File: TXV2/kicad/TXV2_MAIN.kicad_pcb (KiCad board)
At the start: 2 copper layers, 83.3 x 91.7 mm, 58 parts, among them J1 USB-C, J10 TRIMS, J11 WS2812, J12 QWIIC, J13 I2C, J14 RTC, J15 ESP-A, J16 ESP-B, J17 BUZZ, J2 NEXTION, J3 BATT, J4 BAL, J5 BTN, J6 GIMBAL L, J7 GIMBAL R, J8 KNOBS, J9 SWITCHES, U1 Teensy 4.1, U2 ESP32-S3-DevKitC, U3 nRF24 PA/LNA, U4 Pololu 2808, U5 5V buck, U7 BQ25887, U8 AMS1117-3.3

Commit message: TXV2 rev-A: assembly-clarity silk — USB-end arrows + pin-1 markers on both MCUs, per-pin function labels (Nextion GND/skip/5V/RX/TX, buck VIN/GND/VOUT, XT30 +/-), spare headers renamed 'ESP32 SPARE GPIO A/B', Pololu flagged CHECK PINOUT
Co-Authored-By: Claude Fable 5 <noreply@anthropic.com>
Claude-Session: https://claude.ai/code/session_01DvvNNevU4xtNTYtdVBAM7h
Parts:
- J15: value ESP-A -> ESP32 SPARE GPIO (A)
- J16: value ESP-B -> ESP32 SPARE GPIO (B)
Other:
- board text added: "(skip)"
- board text added: "+"
- board text added: "-"
- board text added: "1"
- board text added: "2"
- board text added: "3"
- board text added: "3V3"
- board text added: "4"
- board text added: "5"
- board text added: "5V"
- board text added: "6"
- board text added: "7"
- board text added: "8"
- board text added: "<<< USB END (ESP32)"
- board text added: "<<< USB END (TEENSY)"
- board text added: "BTN"
- board text added: "BUZ"
- board text added: "G"
- board text added: "GND"
- board text added: "LED"
- board text added: "MID"
- board text added: "PWR LATCH - CHECK PINOUT"
- board text added: "RX"
- board text added: "SCL"
- board text added: "SDA"
- board text added: "TX"
- board text added: "VB"
- board text added: "VIN"
- board text added: "VOUT"

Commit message: TXV2 rev-A: corrected board routed (keyed 2808 + dual buck split rail), function-name silk re-applied
Co-Authored-By: Claude Fable 5 <noreply@anthropic.com>
Claude-Session: https://claude.ai/code/session_01DvvNNevU4xtNTYtdVBAM7h
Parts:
- added R17: 47k, Resistor_SMD:R_0805_2012Metric, F.Cu at (116.0, 166.0)
- added R18: 15k, Resistor_SMD:R_0805_2012Metric, F.Cu at (116.0, 170.0)
- added U9: 5V buck NEXT, TXV2:Buck3pin_VGV, F.Cu at (111.0, 172.0)
- U5: value 5V buck -> 5V buck MAIN; footprint TXV2:Buck5V_Socket -> TXV2:Buck3pin_VGV
- moved U5 7.62 mm to (111.0, 164.0), turned to 90 degrees
- moved C11 6.40 mm to (122.0, 142.0)
- moved R15 5.00 mm to (116.0, 142.0)
- moved R16 4.47 mm to (119.0, 142.0)
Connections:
- J1 pad SH: GND -> (no net)
- J2 pad 3: +5V -> +5V_NEXT
- U4 pad 2: GND -> VBAT_RAW
- U4 pad 3: VBAT_SW -> GND
- U4 pad 4: PWRBTN -> GND
- U4 pad 5: (no net) -> PWR_ON
- U4 pad 6: (no net) -> LATCH_OFF
- U4 pad 7: LATCH_OFF -> CTRL_TP
- U4 pad 8: (no net) -> VBAT_SW
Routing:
- net TRIM7: track 116.0 -> 0.00 mm, vias 5 -> 0
- net I2C_SCL: track 240.0 -> 138.0 mm
- net +5V_NEXT: track 0.00 -> 96.3 mm, vias 0 -> 2
- net CHG_STAT: track 73.1 -> 0.00 mm, vias 5 -> 0
- net TRIM8: track 114.0 -> 45.2 mm, vias 6 -> 0
- net LINK_TX2: track 82.2 -> 23.0 mm, vias 3 -> 0
- net VBAT_SW: track 38.6 -> 86.1 mm
- net CHG_TS: track 96.9 -> 50.0 mm, vias 6 -> 4
- net GND: track 38.8 -> 0.00 mm, vias 189 -> 0
- net +3V3_T: track 236.0 -> 203.7 mm
- net PWR_ON: track 0.00 -> 25.3 mm, vias 0 -> 1
- net TRIM6: track 95.7 -> 70.7 mm, vias 5 -> 6
- net PWRBTN: track 92.1 -> 114.6 mm
- net CB_PATH: track 24.0 -> 3.50 mm, vias 2 -> 0
- net I2C_SDA: track 114.7 -> 134.8 mm, vias 7 -> 4
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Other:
- board text added: "PWR LATCH (2808)"
- board text removed: "PWR LATCH - CHECK PINOUT"

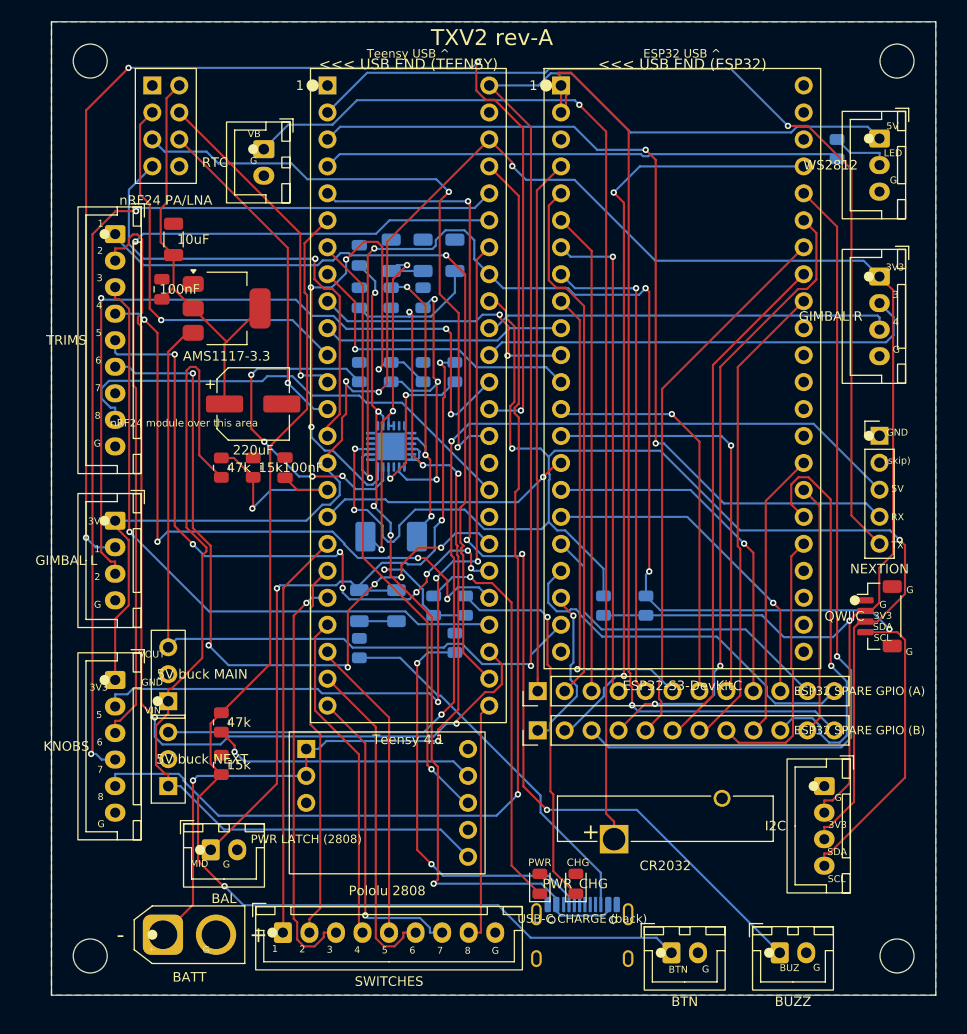
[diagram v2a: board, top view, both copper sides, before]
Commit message: TXV2 rev-A: complete design incl. soft-power diodes, routed ~95% (last ~11 short links + GND stitch for interactive finish before gerbers)
Co-Authored-By: Claude Fable 5 <noreply@anthropic.com>
Claude-Session: https://claude.ai/code/session_01DvvNNevU4xtNTYtdVBAM7h
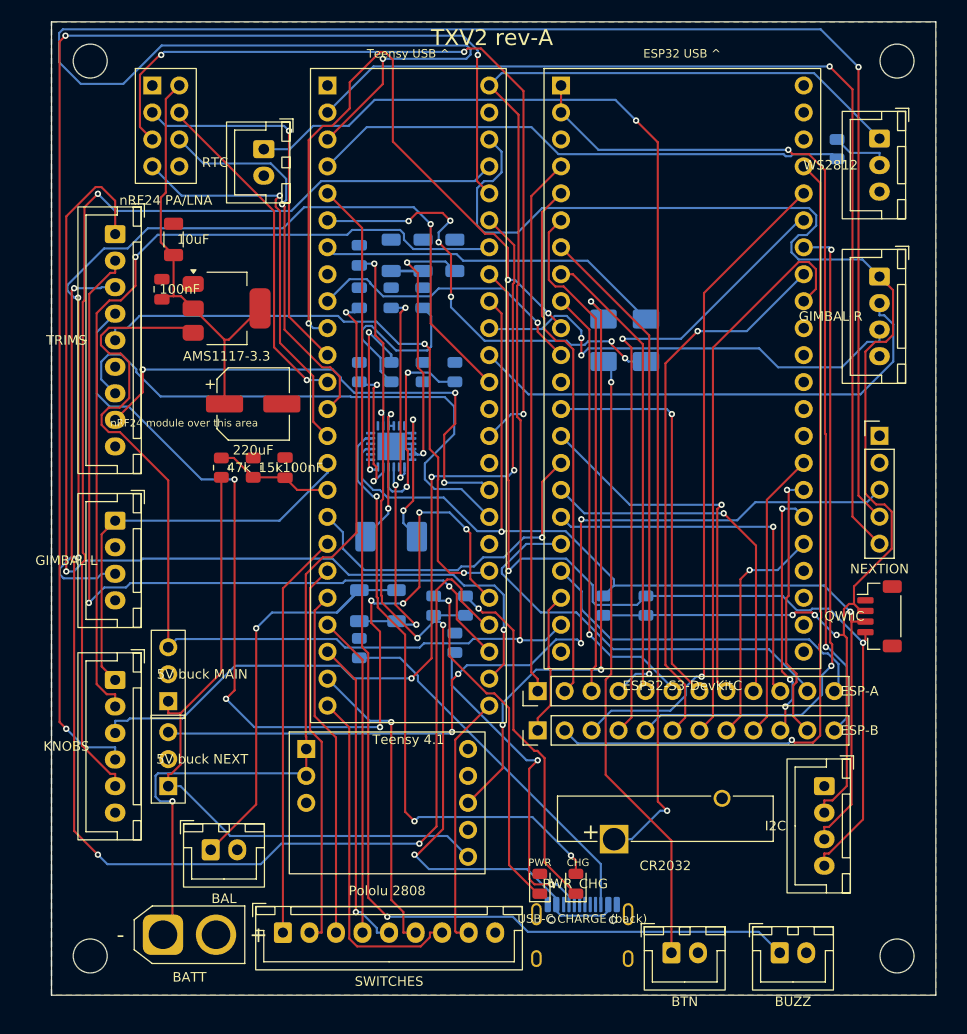
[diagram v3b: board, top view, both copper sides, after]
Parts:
- removed R17: 47k, Resistor_SMD:R_0805_2012Metric
- removed R18: 15k, Resistor_SMD:R_0805_2012Metric
- added D3: 1N4001, Diode_SMD:D_SMA, B.Cu at (154.0, 132.0)
- added D4: 1N4001, Diode_SMD:D_SMA, B.Cu at (154.0, 128.0)
- J15: value ESP32 SPARE GPIO (A) -> ESP-A
- J16: value ESP32 SPARE GPIO (B) -> ESP-B
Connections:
- U1 pad 6: PWRBTN -> BTN_SENSE
- U4 pad 5: PWR_ON -> (no net)
- U4 pad 6: LATCH_OFF -> OFF_2808
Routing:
- net GIMBAL1: track 120.5 -> 0.00 mm, vias 4 -> 0
- net NEXTION_RX: track 83.4 -> 182.8 mm
- net TRIM6: track 70.7 -> 0.00 mm, vias 6 -> 0
- net TRIM3: track 61.4 -> 122.2 mm, vias 1 -> 3
- net OFF_2808: track 0.00 -> 58.5 mm, vias 0 -> 3
- net CHG_STAT: track 0.00 -> 57.6 mm, vias 0 -> 3
- net PWRBTN: track 114.6 -> 58.8 mm
- net TRIM7: track 0.00 -> 54.8 mm
- net I2C_SCL: track 138.0 -> 91.5 mm, vias 5 -> 2
- net BTN_SENSE: track 0.00 -> 42.2 mm, vias 0 -> 6
- net LINK_TX2: track 23.0 -> 65.1 mm, vias 0 -> 3
- net TRIM4: track 61.0 -> 98.2 mm, vias 4 -> 7
- net KNOB7: track 90.5 -> 125.7 mm, vias 2 -> 3
- net I2C_SDA: track 134.8 -> 102.7 mm, vias 4 -> 2
- net CHG_TS: track 50.0 -> 18.3 mm, vias 4 -> 2
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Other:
- board text removed: "(skip)"
- board text removed: "+"
- board text removed: "-"
- board text removed: "1"
- board text removed: "2"
- board text removed: "3"
- board text removed: "3V3"
- board text removed: "4"
- board text removed: "5"
- board text removed: "5V"
- board text removed: "6"
- board text removed: "7"
- board text removed: "8"
- board text removed: "<<< USB END (ESP32)"
- board text removed: "<<< USB END (TEENSY)"
- board text removed: "BTN"
- board text removed: "BUZ"
- board text removed: "G"
- board text removed: "GND"
- board text removed: "LED"
- board text removed: "MID"
- board text removed: "PWR LATCH (2808)"
- board text removed: "RX"
- board text removed: "SCL"
- board text removed: "SDA"
- board text removed: "TX"
- board text removed: "VB"
- board text removed: "VIN"
- board text removed: "VOUT"

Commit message: TXV2 rev-A: routed state (autorouter leaves ~20 links on dense 2-layer; 4-layer recommended)
Co-Authored-By: Claude Fable 5 <noreply@anthropic.com>
Claude-Session: https://claude.ai/code/session_01DvvNNevU4xtNTYtdVBAM7h
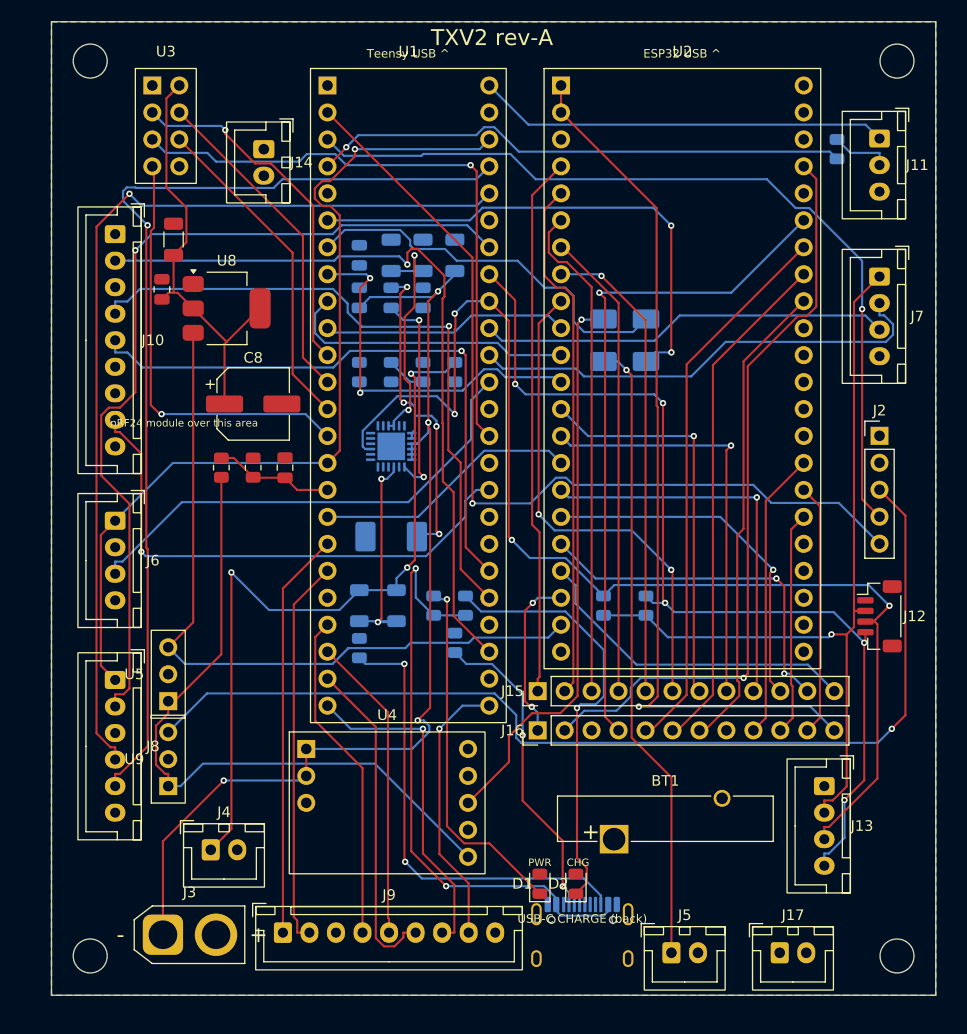
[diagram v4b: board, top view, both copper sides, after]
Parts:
- J3: footprint Connector_AMASS:AMASS_XT30U-M_1x02_P5.0mm_Vertical -> Connector_AMASS:AMASS_XT30U-F_1x02_P5.0mm_Vertical
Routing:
- net TRIM3: track 122.2 -> 0.00 mm, vias 3 -> 0
- net RTC_VBAT: track 110.1 -> 0.00 mm, vias 2 -> 0
- net BUZZER: track 108.9 -> 0.00 mm, vias 1 -> 0
- net NEXTION_RX: track 182.8 -> 80.0 mm, vias 2 -> 1
- net TRIM1: track 94.5 -> 0.00 mm, vias 2 -> 0
- net KNOB6: track 84.1 -> 0.00 mm, vias 3 -> 0
- net +5V: track 177.2 -> 108.6 mm, vias 1 -> 0
- net ESP_G2: track 62.4 -> 0.00 mm, vias 1 -> 0
- net CHG_STAT: track 57.6 -> 0.00 mm, vias 3 -> 0
- net TRIM7: track 54.8 -> 0.00 mm
- net GIMBAL2: track 89.7 -> 45.6 mm, vias 3 -> 0
- net LINK_TX2: track 65.1 -> 23.3 mm, vias 3 -> 0
- net TRIM4: track 98.2 -> 62.3 mm, vias 7 -> 1
- net HANDSHAKE_A: track 0.00 -> 35.7 mm, vias 0 -> 2
- net KNOB7: track 125.7 -> 90.4 mm, vias 3 -> 1
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
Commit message: TXV2 rev-A: 4-LAYER (GND plane In1) - ALL signals routed cleanly; charger-corner GND + diodes = final hand-finish
Co-Authored-By: Claude Fable 5 <noreply@anthropic.com>
Claude-Session: https://claude.ai/code/session_01DvvNNevU4xtNTYtdVBAM7h
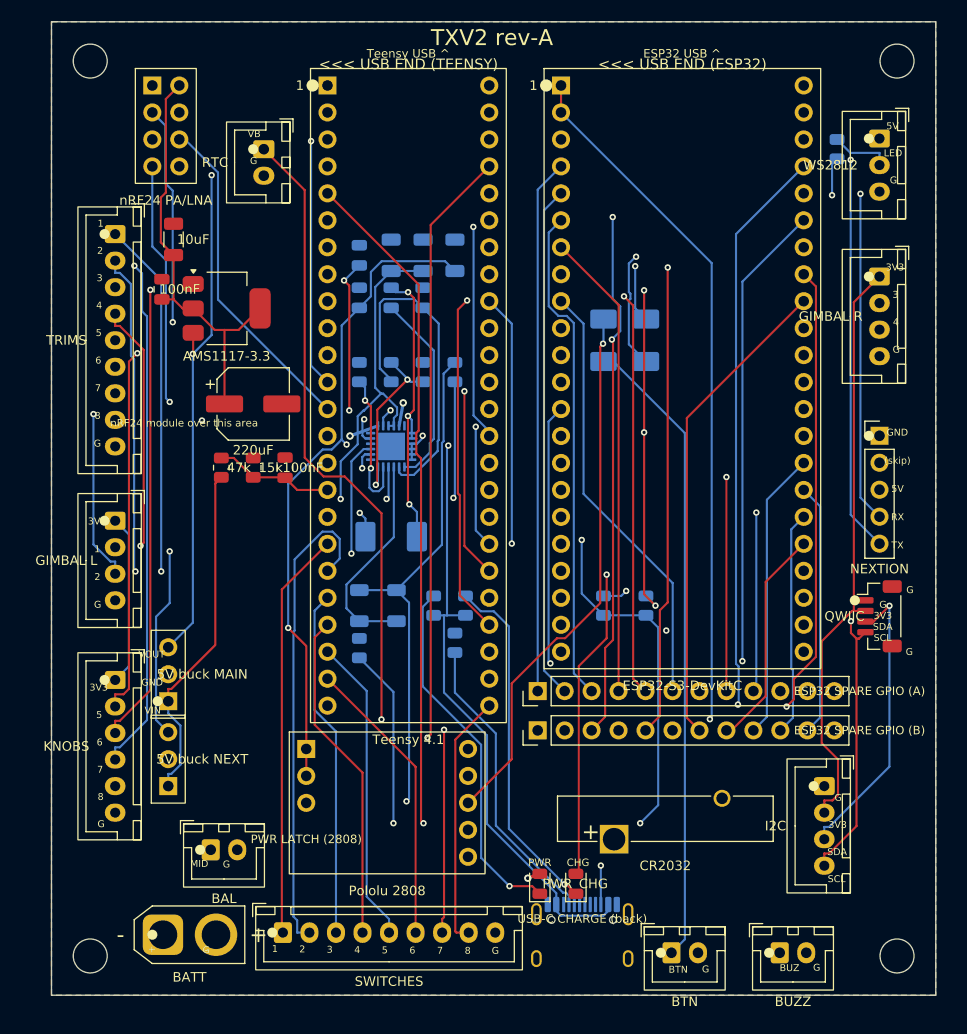
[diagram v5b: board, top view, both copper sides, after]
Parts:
- J15: value ESP-A -> ESP32 SPARE GPIO (A)
- J16: value ESP-B -> ESP32 SPARE GPIO (B)
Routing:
- net BUZZER: track 0.00 -> 101.9 mm, vias 0 -> 1
- net RTC_VBAT: track 0.00 -> 86.1 mm, vias 0 -> 1
- net KNOB6: track 0.00 -> 78.0 mm, vias 0 -> 1
- net TRIM1: track 0.00 -> 68.8 mm, vias 0 -> 1
- net ESP_G2: track 0.00 -> 68.8 mm, vias 0 -> 2
- net TRIM3: track 0.00 -> 67.8 mm, vias 0 -> 1
- net CHG_STAT: track 0.00 -> 62.4 mm, vias 0 -> 2
- net +3V3_T: track 163.0 -> 214.2 mm
- net TRIM6: track 0.00 -> 48.6 mm, vias 0 -> 1
- net +5V: track 108.6 -> 157.0 mm, vias 0 -> 2
- net GIMBAL1: track 0.00 -> 41.5 mm
- net TRIM7: track 0.00 -> 40.8 mm
- net SW3: track 0.00 -> 32.9 mm
- net REGN: track 0.00 -> 31.8 mm
- net I2C_SCL: track 91.2 -> 122.5 mm
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- added copper zone on In1.Cu, net GND
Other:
- copper layers 2 -> 4
- board text added: "(skip)"
- board text added: "+"
- board text added: "-"
- board text added: "1"
- board text added: "2"
- board text added: "3"
- board text added: "3V3"
- board text added: "4"
- board text added: "5"
- board text added: "5V"
- board text added: "6"
- board text added: "7"
- board text added: "8"
- board text added: "<<< USB END (ESP32)"
- board text added: "<<< USB END (TEENSY)"
- board text added: "BTN"
- board text added: "BUZ"
- board text added: "G"
- board text added: "GND"
- board text added: "LED"
- board text added: "MID"
- board text added: "PWR LATCH (2808)"
- board text added: "RX"
- board text added: "SCL"
- board text added: "SDA"
- board text added: "TX"
- board text added: "VB"
- board text added: "VIN"
- board text added: "VOUT"

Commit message: TXV2 rev-A 4-layer checkpoint: clean GND plane, charger grounded (thermal-via EP + local pour), 98% routed (7 items in charger corner + diodes for final interactive pass)
Co-Authored-By: Claude Fable 5 <noreply@anthropic.com>
Claude-Session: https://claude.ai/code/session_01DvvNNevU4xtNTYtdVBAM7h
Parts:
- U7: footprint Package_DFN_QFN:HVQFN-24-1EP_4x4mm_P0.5mm_EP2.6x2.6mm -> Package_DFN_QFN:HVQFN-24-1EP_4x4mm_P0.5mm_EP2.6x2.6mm_ThermalVias
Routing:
- net I2C_SCL: track 122.5 -> 97.6 mm, vias 5 -> 4
- net SPI_SCK: track 54.0 -> 74.5 mm, vias 1 -> 2
- net +3V3_T: track 214.2 -> 232.0 mm, vias 2 -> 7
- net VBAT_RAW: track 93.2 -> 108.0 mm
- net CHG_ILIM: track 14.0 -> 0.00 mm, vias 2 -> 0
- net ESP_3V3: track 77.9 -> 91.3 mm
- net TRIM4: track 58.3 -> 71.3 mm
- net TRIM1: track 68.8 -> 80.2 mm
- net TRIM2: track 67.0 -> 77.8 mm, vias 1 -> 3
- net LINK_TX2: track 23.0 -> 33.2 mm
- net OFF_2808: track 51.3 -> 60.6 mm, vias 1 -> 2
- net SW2: track 45.6 -> 36.7 mm
- net ESP_G4: track 50.3 -> 57.5 mm
- net BUZZER: track 101.9 -> 109.0 mm, vias 1 -> 2
- net KNOB8: track 88.2 -> 95.2 mm
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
